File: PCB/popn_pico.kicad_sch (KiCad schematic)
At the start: 35 parts, among them SW1 KAN4542-0701C, SW2 KAN4542-0701C, U1 Pico

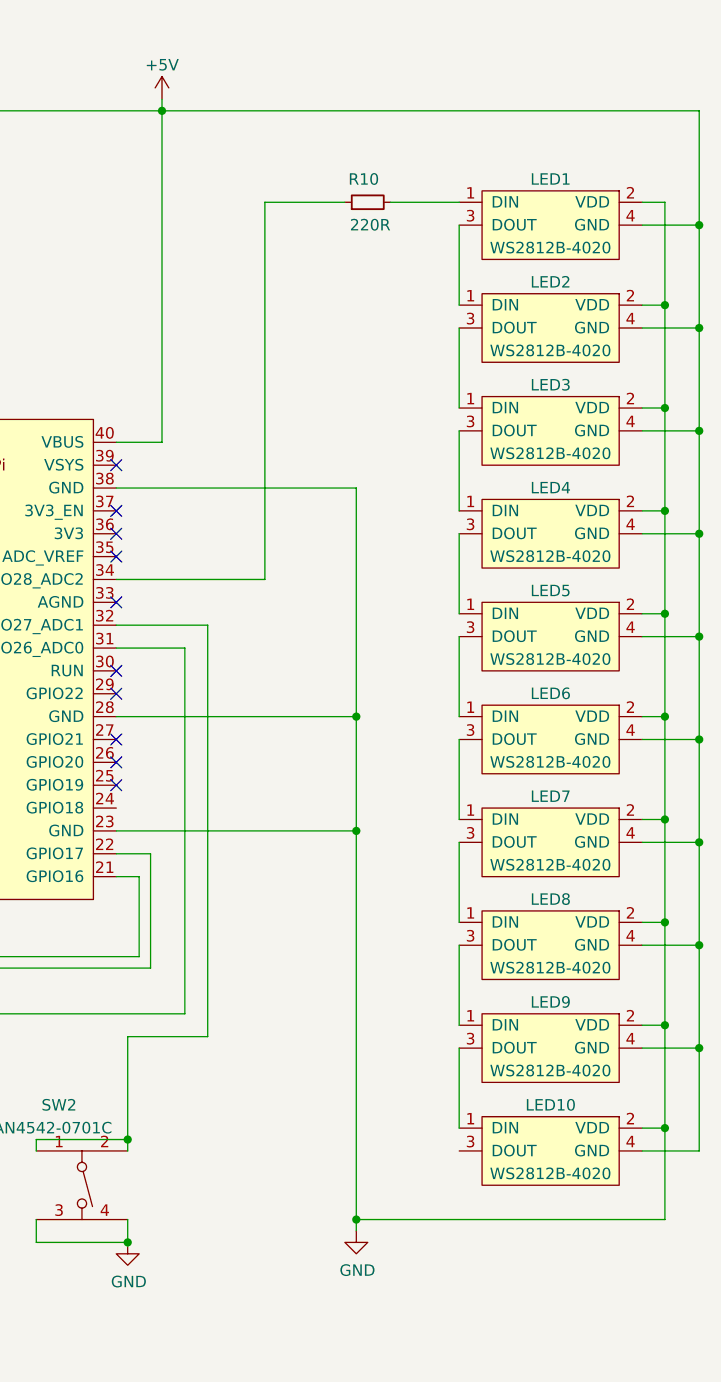
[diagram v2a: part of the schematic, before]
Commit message: Fixed PCB bug (LED 5v and GND swapped)
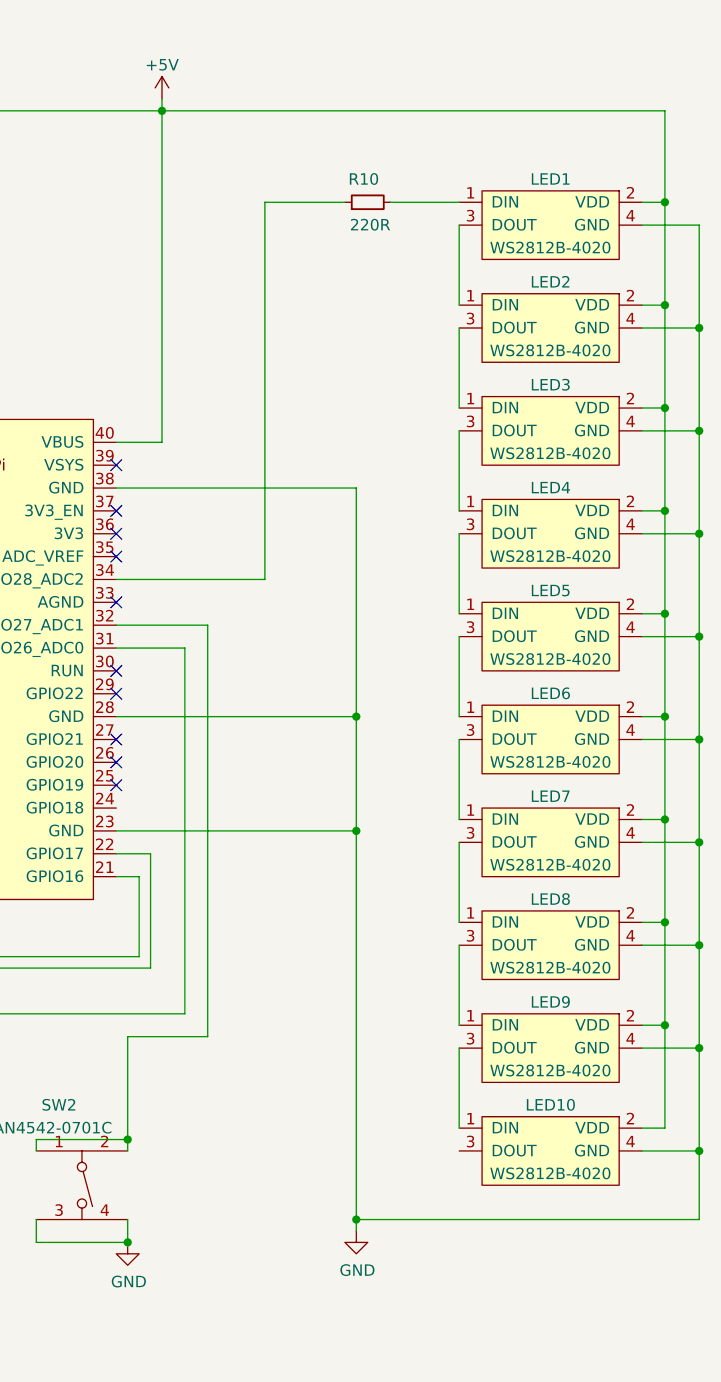
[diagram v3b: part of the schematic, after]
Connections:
- net +5V: now also LED1.2 (VDD), LED10.2 (VDD), LED2.2 (VDD), LED3.2 (VDD), LED4.2 (VDD), LED5.2 (VDD), LED6.2 (VDD), LED7.2 (VDD), LED8.2 (VDD), LED9.2 (VDD); no longer LED1.4 (GND), LED10.4 (GND), LED2.4 (GND), LED3.4 (GND), LED4.4 (GND), LED5.4 (GND), LED6.4 (GND), LED7.4 (GND), LED8.4 (GND), LED9.4 (GND)
- net GND: now also LED1.4 (GND), LED10.4 (GND), LED2.4 (GND), LED3.4 (GND), LED4.4 (GND), LED5.4 (GND), LED6.4 (GND), LED7.4 (GND), LED8.4 (GND), LED9.4 (GND); no longer LED1.2 (VDD), LED10.2 (VDD), LED2.2 (VDD), LED3.2 (VDD), LED4.2 (VDD), LED5.2 (VDD), LED6.2 (VDD), LED7.2 (VDD), LED8.2 (VDD), LED9.2 (VDD)
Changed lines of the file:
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@@
   (junction (at 95.25 180.34) (diameter 0) (color 0 0 0 0)
   )
+  (junction (at 262.89 143.51) (diameter 0) (color 0 0 0 0)
+  )
   (junction (at 99.06 27.94) (diameter 0) (color 0 0 0 0)
   )
@@
   (junction (at 71.12 156.21) (diameter 0) (color 0 0 0 0)
   )
-  (junction (at 259.08 140.97) (diameter 0) (color 0 0 0 0)
-  )
   (junction (at 259.08 72.39) (diameter 0) (color 0 0 0 0)
   )
   (junction (at 259.08 118.11) (diameter 0) (color 0 0 0 0)
   )
+  (junction (at 259.08 38.1) (diameter 0) (color 0 0 0 0)
+  )
   (junction (at 85.09 171.45) (diameter 0) (color 0 0 0 0)
-  )
-  (junction (at 262.89 40.64) (diameter 0) (color 0 0 0 0)
   )
   (junction (at 262.89 132.08) (diameter 0) (color 0 0 0 0)
@@
     (stroke (width 0) (type default) (color 0 0 0 0))
   )
-  (wire (pts (xy 259.08 140.97) (xy 259.08 151.13))
-    (stroke (width 0) (type default) (color 0 0 0 0))
-  )
   (wire (pts (xy 72.39 156.21) (xy 71.12 156.21))
     (stroke (width 0) (type default) (color 0 0 0 0))
@@
     (stroke (width 0) (type default) (color 0 0 0 0))
   )
+  (wire (pts (xy 262.89 151.13) (xy 262.89 143.51))
+    (stroke (width 0) (type default) (color 0 0 0 0))
+  )
   (wire (pts (xy 262.89 74.93) (xy 262.89 86.36))
     (stroke (width 0) (type default) (color 0 0 0 0))
@@
     (stroke (width 0) (type default) (color 0 0 0 0))
   )
-  (wire (pts (xy 262.89 27.94) (xy 262.89 40.64))
-    (stroke (width 0) (type default) (color 0 0 0 0))
-  )
   (wire (pts (xy 127 156.21) (xy 124.46 156.21))
     (stroke (width 0) (type default) (color 0 0 0 0))
@@
     (stroke (width 0) (type default) (color 0 0 0 0))
   )
-  (wire (pts (xy 224.79 151.13) (xy 259.08 151.13))
+  (wire (pts (xy 259.08 27.94) (xy 203.2 27.94))
+    (stroke (width 0) (type default) (color 0 0 0 0))
+  )
+  (wire (pts (xy 224.79 151.13) (xy 262.89 151.13))
     (stroke (width 0) (type default) (color 0 0 0 0))
   )
@@
     (stroke (width 0) (type default) (color 0 0 0 0))
   )
-  (wire (pts (xy 203.2 27.94) (xy 262.89 27.94))
-    (stroke (width 0) (type default) (color 0 0 0 0))
-  )
   (wire (pts (xy 90.17 90.17) (xy 90.17 166.37))
     (stroke (width 0) (type default) (color 0 0 0 0))
@@
     (stroke (width 0) (type default) (color 0 0 0 0))
   )
+  (wire (pts (xy 259.08 38.1) (xy 259.08 27.94))
+    (stroke (width 0) (type default) (color 0 0 0 0))
+  )

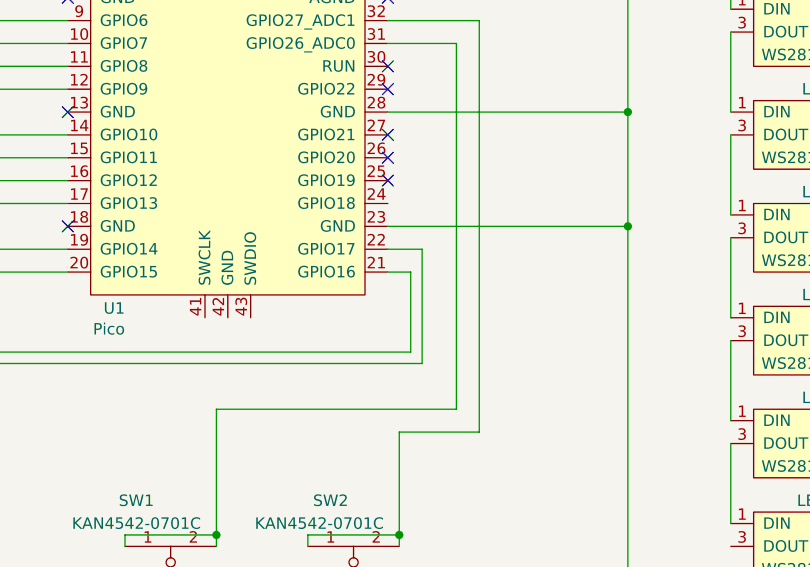
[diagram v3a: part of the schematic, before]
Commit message: LED9 pin changed to support PWM, UF2 firmware updated too
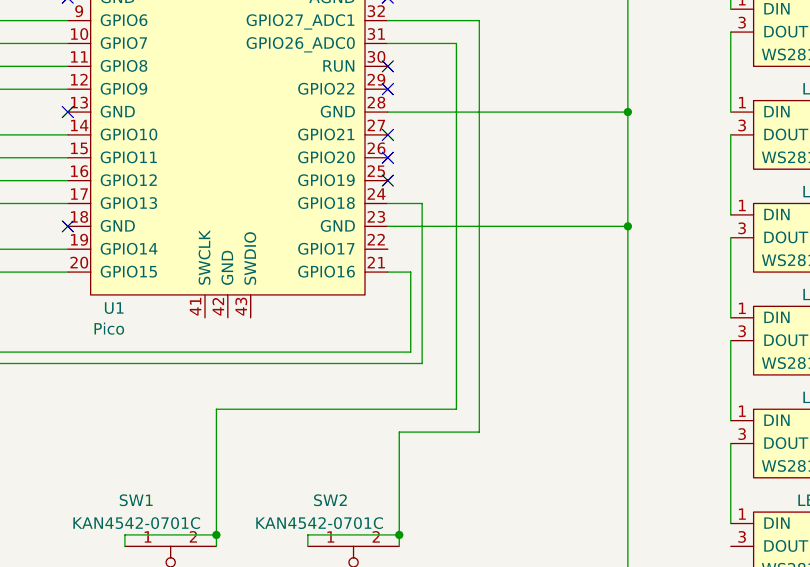
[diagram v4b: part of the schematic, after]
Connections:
- net at U1.22 (GPIO17): no longer R9.1
- net at U1.24 (GPIO18): now also R9.1
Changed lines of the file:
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@@
-    (stroke (width 0) (type default) (color 0 0 0 0))
-  )
-  (wire (pts (xy 201.93 110.49) (xy 198.12 110.49))
     (stroke (width 0) (type default) (color 0 0 0 0))
   )
@@
     (stroke (width 0) (type default) (color 0 0 0 0))
   )
-  (wire (pts (xy 201.93 123.19) (xy 201.93 110.49))
+  (wire (pts (xy 201.93 105.41) (xy 201.93 123.19))
     (stroke (width 0) (type default) (color 0 0 0 0))
   )
@@
     (stroke (width 0) (type default) (color 0 0 0 0))
   )
+  (wire (pts (xy 198.12 105.41) (xy 201.93 105.41))
+    (stroke (width 0) (type default) (color 0 0 0 0))
+  )
